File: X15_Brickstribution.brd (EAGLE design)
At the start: 152.4 x 76.2 mm, 77 parts, among them J1 IPL1-104-01-X-S-K, U5 IC_L4970A, U6 DIODE_STPS1545CT, U7 IC_L4970A, U8 DIODE_STPS1545CT

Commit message: In progress board
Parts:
- removed R31: DIODE_RBQ30NS45AFHTL, X15_Brickstribution:TRANS_R5009FNJ_ROM
- removed REV_TRANS: TRANS_IRF1018E_S_SLPBF, X15_Brickstribution:IRF1018E_S_SLPBF
- added R2: DIODE_RBQ30NS45AFHTL, X15_Brickstribution:TRANS_R5009FNJ_ROM
- added U$3: TRANS_IRF1018EPBF, X15_Brickstribution:D2PAK
- moved R21 115.0 mm to (177.6, 4.19), turned to 270 degrees
- moved C30 113.2 mm to (184.8, 16.0)
- moved D14 113.2 mm to (176.5, 7.11)
- moved R8 113.2 mm to (161.5, 63.8)
- moved +7.4VOUT1_TEST 113.2 mm to (206.0, 63.8)
- moved +7.4VOUT2_TEST 113.2 mm to (202.2, 63.7)
- moved 48V_GND_TEST 113.2 mm to (153.5, 63.7)
- moved 48V_TEST 113.2 mm to (166.9, 63.7)
- moved D12 113.2 mm to (172.9, 4.75)
- moved D13 113.2 mm to (200.7, 38.0)
- moved D8 113.2 mm to (157.8, 63.8)
- moved R22 113.2 mm to (201.5, 35.1)
- moved R12 112.7 mm to (175.9, 9.14)
- moved C38 69.4 mm to (27.9, 49.4), turned to 180 degrees
- moved C39 66.3 mm to (32.8, 41.0), turned to 0 degrees
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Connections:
- net +12V_CONV: no longer U5.9, U7.9
- net +48V: now also C1.1, C2.1, C3.1, U5.9, U7.9; no longer C1.2, C2.2, C3.2
- net +7.4V_SERVO: now also R2.2; no longer R31.2
- net 12V_GND: no longer 7.4V_GND.1, C23.1, C24.1, C26.1, C27.1, C28.1, C29.2, C30.1, C32.1, C33.1, C35.1, C36.1, C37.1, C38.2, C39.1, D12.C, D14.C, J1.03, J1.04, R23.1, R24.1, R26.1, R27.1, R28.1, R30.1, U5.3, U5.8, U6.1, U6.3, U7.3, U7.8, U8.1, U8.3
- net 48V_GND: now also 7.4V_GND.1, C1.2, C2.2, C23.1, C24.1, C26.1, C27.1, C28.1, C29.2, C3.2, C30.1, C32.1, C33.1, C35.1, C36.1, C37.1, C38.2, C39.1, D12.C, D14.C, J1.03, J1.04, R23.1, R24.1, R26.1, R27.1, R28.1, R30.1, U$3.2, U5.16, U5.3, U5.8, U6.1, U6.3, U7.16, U7.3, U7.8, U8.1, U8.3; no longer C1.1, C2.1, C3.1, REV_TRANS.P$3
- net GND_RAW: now also U$3.3; no longer REV_TRANS.P$2
- net REV_GATE: now also U$3.1; no longer REV_TRANS.P$1
- net VOUT1: now also R2.3; no longer R31.3
- net VOUT2: now also R2.1; no longer R31.1
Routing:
- net VOUT1: track 98.4 -> 15.0 mm, vias 1 -> 0
- net VOUT2: track 114.0 -> 45.0 mm, vias 1 -> 0
- net +3.3V: track 49.1 -> 0.00 mm
- net OUT2: track 84.0 -> 39.9 mm
- net +5V: track 35.8 -> 0.00 mm
- net OUT1: track 80.8 -> 55.1 mm
- net 48V_GND: track 3.57 -> 12.8 mm, vias 0 -> 3
- net +12V_CONV: track 8.76 -> 0.00 mm, vias 1 -> 0
- net BOOT2: track 20.8 -> 15.0 mm
- net FCOMP2: track 15.4 -> 20.0 mm
- net +12V: track 4.19 -> 0.00 mm
- net SS1: track 22.0 -> 25.6 mm
- net BOOT_1: track 10.8 -> 13.7 mm
- net C_OSC2: track 26.4 -> 23.7 mm
- net VSTART1: track 5.71 -> 3.21 mm
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- added copper zone on layer 1, net 48V_GND
- removed copper zone on layer 16, net +7.4V_SERVO
- removed copper zone on layer 1, net 12V_GND
- removed copper zone on layer 16, net 48V_GND

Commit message: Finished version of alternative layout
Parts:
- moved +7.4VOUT1_TEST 206.1 mm to (2.29, 32.8)
- moved +7.4VOUT2_TEST 157.8 mm to (44.7, 74.1)
- moved D14 151.3 mm to (25.3, 15.2)
- moved R12 146.3 mm to (29.8, 15.2), turned to 180 degrees
- moved C30 142.7 mm to (42.2, 21.7), turned to 180 degrees
- moved R21 141.5 mm to (36.8, 17.1), turned to 90 degrees
- moved D12 138.2 mm to (35.7, 21.3)
- moved D8 118.4 mm to (40.9, 44.7)
- moved R8 117.6 mm to (45.4, 44.7)
- moved R22 102.3 mm to (99.3, 31.6), turned to 270 degrees
- moved D13 102.0 mm to (99.3, 27.1), turned to 270 degrees
- moved 48V_TEST 89.3 mm to (78.3, 74.1)
- moved 48V_GND_TEST 70.9 mm to (83.4, 74.1)
- moved +7.4V_SERVO_TEST 14.5 mm to (28.8, 2.62)
- moved U$2 9.65 mm to (44.6, 67.6)
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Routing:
- net VOUT1: track 15.0 -> 63.2 mm, vias 0 -> 1
- net +3.3V: track 0.00 -> 45.1 mm
- net +5V: track 0.00 -> 42.8 mm
- net 48V_GND: track 12.8 -> 50.0 mm, vias 3 -> 6
- net VOUT2: track 45.0 -> 73.0 mm, vias 0 -> 2
- net OUT2: track 39.9 -> 54.4 mm, vias 0 -> 2
- net +12V_CONV: track 0.00 -> 5.06 mm, vias 0 -> 1
- net +12V: track 0.00 -> 4.92 mm
- net +48V: track 6.06 -> 10.6 mm
- net N$12: track 0.00 -> 3.32 mm
- net N$13: track 0.00 -> 2.82 mm
- net N$11: track 0.00 -> 2.74 mm
- net N$4: track 0.00 -> 2.74 mm
- net VREF1: track 9.62 -> 11.8 mm
- net N$9: track 0.00 -> 2.11 mm
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- added copper zone on layer 1, net +7.4V_SERVO
- added copper zone on layer 1, net 12V_GND

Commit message: Alumni Revisions Implemented
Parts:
- removed D2: SK34A-TPDO-214AC_HSMA_MCC-M, X15_Brickstribution:DO-214AC_HSMA_MCC-M
- removed D9: GREEN, SparkFun-LED:LED-0603
- removed R9: 470, SparkFun-Resistors:0603
- added CR1: Zener, X15_Brickstribution:DIODE_DO-214AA_4P38X3P62_MCC-M
- moved 12V_GND_TEST 37.0 mm to (150.3, 37.3)
- moved +12V_TEST 35.0 mm to (150.1, 33.7)
- moved 3.3V_GND 17.0 mm to (150.2, 30.4)
- moved 5V_GND 12.7 mm to (150.2, 23.2)
- moved +3.3V_TEST 3.30 mm to (150.1, 26.3)
- moved D10 0.76 mm to (142.4, 8.86)
- moved D11 0.76 mm to (139.8, 8.86)
- moved R10 0.51 mm to (142.4, 13.0)
- moved R11 0.51 mm to (139.8, 13.0)
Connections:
- removed net +12V_CONV: +12V_TEST.1, BACKPLANE_CONN.07, BACKPLANE_POWER.1@1, BACKPLANE_POWER.1@2, BACKPLANE_POWER.1@3, BACKPLANE_POWER.1@4, BACKPLANE_POWER.1@5, BACKPLANE_POWER.1@6, BACKPLANE_POWER.2@1, BACKPLANE_POWER.2@2, BACKPLANE_POWER.2@3, BACKPLANE_POWER.2@4, BACKPLANE_POWER.2@5, BACKPLANE_POWER.2@6, BACKPLANE_POWER.3@1, BACKPLANE_POWER.3@2, BACKPLANE_POWER.3@3, BACKPLANE_POWER.3@4, BACKPLANE_POWER.3@5, BACKPLANE_POWER.3@6, BACKPLANE_POWER.4@1, BACKPLANE_POWER.4@2, BACKPLANE_POWER.4@3, BACKPLANE_POWER.4@4, BACKPLANE_POWER.4@5, BACKPLANE_POWER.4@6, BACKPLANE_POWER.5@1, BACKPLANE_POWER.5@2, BACKPLANE_POWER.5@3, BACKPLANE_POWER.5@4, BACKPLANE_POWER.5@5, BACKPLANE_POWER.5@6, D2.1, R9.1, U$1.1, U$1.2
- removed net N$8: D9.A, R9.2
- net +12V: now also +12V_TEST.1, BACKPLANE_CONN.07, BACKPLANE_POWER.1@1, BACKPLANE_POWER.1@2, BACKPLANE_POWER.1@3, BACKPLANE_POWER.1@4, BACKPLANE_POWER.1@5, BACKPLANE_POWER.1@6, BACKPLANE_POWER.2@1, BACKPLANE_POWER.2@2, BACKPLANE_POWER.2@3, BACKPLANE_POWER.2@4, BACKPLANE_POWER.2@5, BACKPLANE_POWER.2@6, BACKPLANE_POWER.3@1, BACKPLANE_POWER.3@2, BACKPLANE_POWER.3@3, BACKPLANE_POWER.3@4, BACKPLANE_POWER.3@5, BACKPLANE_POWER.3@6, BACKPLANE_POWER.4@1, BACKPLANE_POWER.4@2, BACKPLANE_POWER.4@3, BACKPLANE_POWER.4@4, BACKPLANE_POWER.4@5, BACKPLANE_POWER.4@6, BACKPLANE_POWER.5@1, BACKPLANE_POWER.5@2, BACKPLANE_POWER.5@3, BACKPLANE_POWER.5@4, BACKPLANE_POWER.5@5, BACKPLANE_POWER.5@6, CR1.1, U$1.1, U$1.2, U$1.3, U$1.4; no longer D2.2
- net 12V_GND: now also CR1.2; no longer D9.C, U$1.3, U$1.4
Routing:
- net +3.3V: track 45.1 -> 50.6 mm
- net +12V_CONV: track 5.06 -> 0.00 mm, vias 1 -> 0
- net +12V: track 4.92 -> 8.91 mm
- net N$8: track 1.88 -> 0.00 mm
- net +5V: track 42.8 -> 43.3 mm
- removed copper zone on layer 16, net +12V_CONV

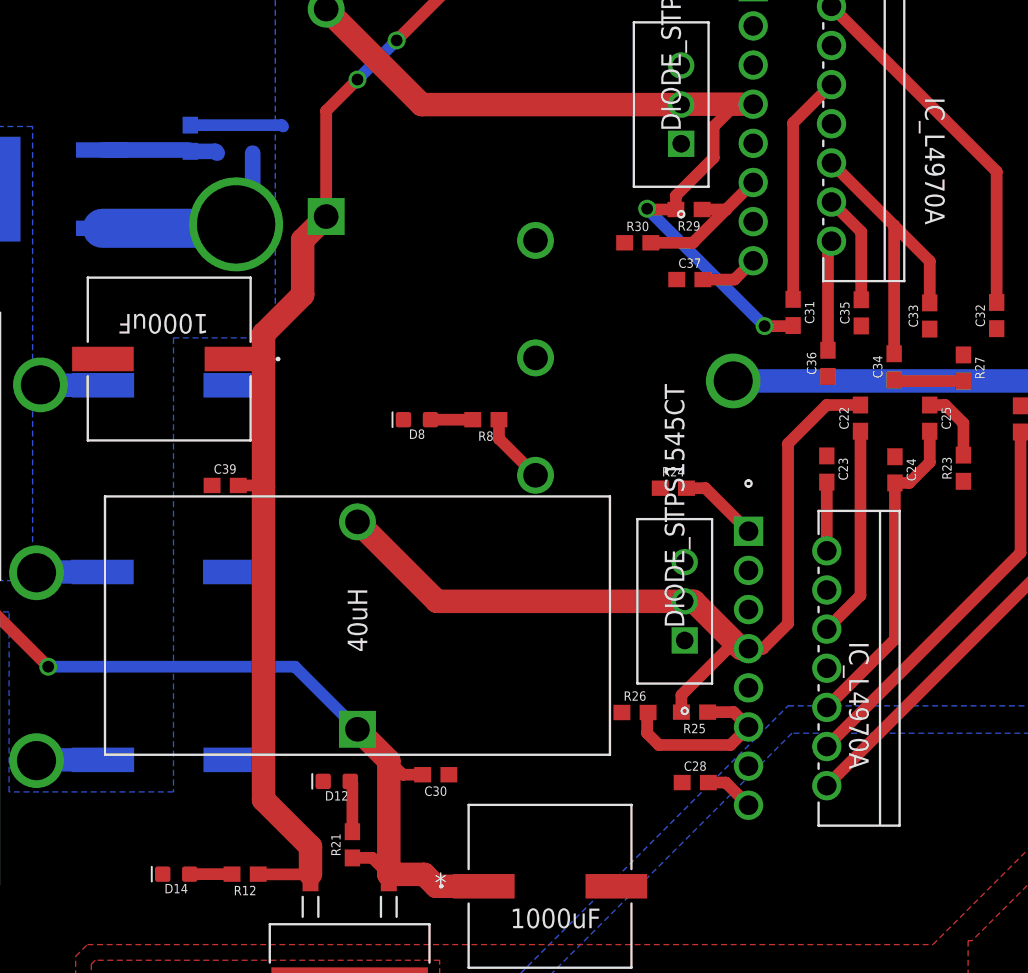
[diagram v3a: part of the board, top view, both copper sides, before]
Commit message: Fixed Tracing Errors
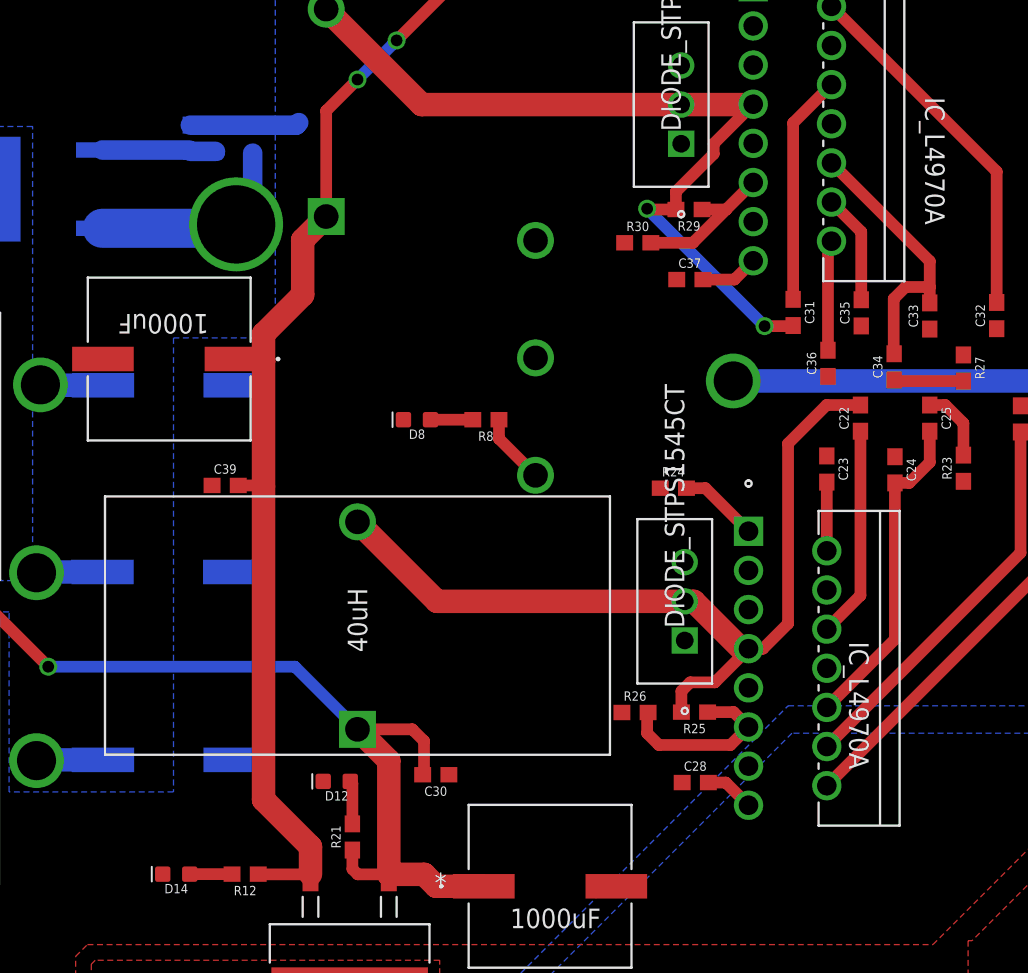
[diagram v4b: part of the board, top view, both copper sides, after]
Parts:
- moved R21 0.51 mm to (36.8, 17.7)
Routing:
- net VOUT1: track 63.2 -> 65.5 mm
- net FCOMP2: track 20.0 -> 18.0 mm
- net +48V: track 10.6 -> 11.7 mm
- net OUT2: track 54.4 -> 53.7 mm
- net OUT1: track 55.7 -> 56.3 mm
- net N$12: track 3.32 -> 2.81 mm
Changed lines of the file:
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@@
 <attribute name="VALUE" x="27.4828" y="1.0922" size="0.6096" layer="27" font="vector" ratio="20" align="top-left"/>
 </element>
-<element name="R21" library="SparkFun-Resistors" library_urn="urn:adsk.eagle:library:532" package="0603" package3d_urn="urn:adsk.eagle:package:39650/1" value="470" x="36.7538" y="17.145" smashed="yes" rot="R90">
-<attribute name="NAME" x="35.9918" y="17.145" size="0.6096" layer="25" font="vector" ratio="20" rot="R90" align="bottom-center"/>
-<attribute name="PROD_ID" value="RES-07869" x="36.7538" y="18.415" size="1.778" layer="27" rot="R90" display="off"/>
-<attribute name="VALUE" x="37.5158" y="17.145" size="0.6096" layer="27" font="vector" ratio="20" rot="R90" align="top-center"/>
+<element name="R21" library="SparkFun-Resistors" library_urn="urn:adsk.eagle:library:532" package="0603" package3d_urn="urn:adsk.eagle:package:39650/1" value="470" x="36.7538" y="17.653" smashed="yes" rot="R90">
+<attribute name="NAME" x="35.9918" y="17.653" size="0.6096" layer="25" font="vector" ratio="20" rot="R90" align="bottom-center"/>
+<attribute name="PROD_ID" value="RES-07869" x="36.7538" y="18.923" size="1.778" layer="27" rot="R90" display="off"/>
+<attribute name="VALUE" x="37.5158" y="17.653" size="0.6096" layer="27" font="vector" ratio="20" rot="R90" align="top-center"/>
 </element>
 <element name="D12" library="SparkFun-LED" library_urn="urn:adsk.eagle:library:529" package="LED-0603" package3d_urn="urn:adsk.eagle:package:39354/1" value="GREEN" x="35.7378" y="21.2598" smashed="yes" rot="R180">
@@
 <vertex x="14.478" y="32.258"/>
 </polygon>
-<wire x1="26.2382" y1="63.842" x2="32.17" y2="63.842" width="0.762" layer="16"/>
-<wire x1="32.17" y1="63.842" x2="32.258" y2="63.754" width="0.762" layer="16"/>
 <wire x1="48.637" y1="41.1202" x2="46.2652" y2="43.492" width="0.762" layer="1"/>
 <wire x1="46.2652" y1="43.492" x2="46.2652" y2="44.7294" width="0.762" layer="1"/>
+<wire x1="26.2382" y1="63.842" x2="33.108" y2="63.842" width="1.27" layer="16"/>
+<wire x1="33.108" y1="63.842" x2="33.274" y2="64.008" width="1.27" layer="16"/>
 </signal>
 <signal name="48V_GND">
@@
 <wire x1="20.522" y1="57.15" x2="28.956" y2="57.15" width="2.54" layer="16"/>
 <wire x1="28.956" y1="57.15" x2="29.21" y2="57.404" width="2.54" layer="16"/>
-<wire x1="30.2838" y1="62.0268" x2="30.2838" y2="58.4778" width="1.016" layer="16"/>
-<wire x1="30.2838" y1="58.4778" x2="28.956" y2="57.15" width="1.016" layer="16"/>
 <wire x1="20.566896875" y1="46.9646" x2="16.5354" y2="46.9646" width="1.524" layer="16"/>
 <wire x1="20.541496875" y1="34.8488" x2="16.3068" y2="34.8488" width="1.524" layer="16"/>
@@
 <vertex x="96.012" y="32.258"/>
 </polygon>
+<wire x1="29.21" y1="57.404" x2="30.2838" y2="58.4778" width="1.27" layer="16"/>
+<wire x1="30.2838" y1="58.4778" x2="30.2838" y2="62.0268" width="1.27" layer="16"/>
 </signal>
 <signal name="12V_GND">
@@
 <contactref element="U$3" pad="1"/>
 <wire x1="26.1502" y1="62.23" x2="26.2382" y2="62.142" width="0.762" layer="16"/>
-<wire x1="20.522" y1="62.23" x2="26.1502" y2="62.23" width="1.016" layer="16"/>
-<wire x1="26.2382" y1="62.142" x2="27.8686" y2="62.142" width="1.016" layer="16"/>
 <wire x1="27.8686" y1="62.142" x2="27.9838" y2="62.0268" width="1.016" layer="16"/>
+<wire x1="20.522" y1="62.23" x2="26.1502" y2="62.23" width="1.27" layer="16"/>
+<wire x1="26.2382" y1="62.142" x2="27.8686" y2="62.142" width="1.27" layer="16"/>
 </signal>
 <signal name="GND_RAW">
@@
 <contactref element="C33" pad="2"/>
 <contactref element="C34" pad="2"/>
-<wire x1="67.8434" y1="61.3918" x2="71.9074" y2="57.3278" width="0.762" layer="1"/>
-<wire x1="71.9074" y1="57.3278" x2="71.9074" y2="49.0084" width="0.762" layer="1"/>
-<wire x1="71.9074" y1="57.3278" x2="74.2188" y2="55.0164" width="0.762" layer="1"/>
-<wire x1="74.2188" y1="55.0164" x2="74.2188" y2="52.3104" width="0.762" layer="1"/>
+<wire x1="67.8434" y1="61.3918" x2="74.2188" y2="55.0164" width="0.762" layer="1"/>
+<wire x1="74.2188" y1="55.0164" x2="74.2188" y2="53.34" width="0.762" layer="1"/>
+<wire x1="74.2188" y1="53.34" x2="74.2188" y2="52.3104" width="0.762" layer="1"/>
+<wire x1="74.2188" y1="53.34" x2="72.644" y2="53.34" width="0.762" layer="1"/>
+<wire x1="72.644" y1="53.34" x2="71.882" y2="52.578" width="0.762" layer="1"/>
+<wire x1="71.882" y1="52.578" x2="71.882" y2="49.0338" width="0.762" layer="1"/>
+<wire x1="71.882" y1="49.0338" x2="71.9074" y2="49.0084" width="0.762" layer="1"/>
 </signal>
 <signal name="R_OSC2">
@@
 <contactref element="L2" pad="2"/>
 <contactref element="R29" pad="2"/>
-<wire x1="57.7478" y1="58.3692" x2="57.7478" y2="59.2718" width="0.762" layer="1"/>
-<wire x1="57.7478" y1="59.2718" x2="60.198" y2="61.722" width="0.762" layer="1"/>
-<wire x1="60.198" y1="61.722" x2="60.198" y2="63.754" width="0.762" layer="1"/>
-<wire x1="60.198" y1="63.754" x2="61.6458" y2="65.2018" width="0.762" layer="1"/>
-<wire x1="61.6458" y1="65.2018" x2="62.7634" y2="65.2018" width="0.762" layer="1"/>
-<wire x1="62.7634" y1="65.2018" x2="58.1152" y2="65.2018" width="1.524" layer="1"/>
-<wire x1="58.1152" y1="65.2018" x2="58.0898" y2="65.1764" width="1.524" layer="1"/>
 <wire x1="58.0898" y1="65.1764" x2="41.2496" y2="65.1764" width="1.524" layer="1"/>
 <wire x1="41.2496" y1="65.1764" x2="35.052" y2="71.374" width="1.524" layer="1"/>
@@
 <wire x1="63.5" y1="50.8" x2="65.3152" y2="50.8" width="0.762" layer="1"/>
 <wire x1="65.3152" y1="50.8" x2="65.3542" y2="50.839" width="0.762" layer="1"/>
+<wire x1="62.738" y1="65.1764" x2="60.198" y2="62.6364" width="0.762" layer="1"/>
+<wire x1="60.198" y1="62.6364" x2="60.198" y2="61.976" width="0.762" layer="1"/>
+<wire x1="60.198" y1="61.976" x2="57.7478" y2="59.5258" width="0.762" layer="1"/>
+<wire x1="57.7478" y1="59.5258" x2="57.7478" y2="58.3692" width="0.762" layer="1"/>
+<wire x1="62.738" y1="65.1764" x2="62.7634" y2="65.2018" width="1.524" layer="1"/>
+<wire x1="58.0898" y1="65.1764" x2="62.738" y2="65.1764" width="1.524" layer="1"/>
 </signal>
 <signal name="VSTART2">
@@
 <wire x1="37.084" y1="24.638" x2="39.116" y2="22.606" width="1.524" layer="1"/>
 <wire x1="39.116" y1="22.606" x2="39.116" y2="15.2273" width="1.524" layer="1"/>
-<wire x1="37.084" y1="24.638" x2="40.0304" y2="21.6916" width="0.762" layer="1"/>
-<wire x1="40.0304" y1="21.6916" x2="41.314" y2="21.6916" width="0.762" layer="1"/>
 <wire x1="37.084" y1="24.638" x2="33.02" y2="28.702" width="0.762" layer="16"/>
 <wire x1="33.02" y1="28.702" x2="17.018" y2="28.702" width="0.762" layer="16"/>
@@
 <wire x1="17.018" y1="28.702" x2="12.9286" y2="32.7914" width="0.762" layer="1"/>
 <wire x1="12.9286" y1="32.7914" x2="2.286" y2="32.7914" width="0.762" layer="1"/>
-<wire x1="39.116" y1="15.2273" x2="38.0483" y2="16.295" width="0.762" layer="1"/>
-<wire x1="38.0483" y1="16.295" x2="36.7538" y2="16.295" width="0.762" layer="1"/>
 <wire x1="39.116" y1="15.2273" x2="41.4147" y2="15.2273" width="1.524" layer="1"/>
 <wire x1="42.1894" y1="14.4526" x2="45.281096875" y2="14.4526" width="1.524" layer="1"/>
 <wire x1="41.4147" y1="15.2273" x2="42.1894" y2="14.4526" width="1.524" layer="1"/>
+<wire x1="37.084" y1="24.638" x2="40.64" y2="24.638" width="0.762" layer="1"/>
+<wire x1="40.64" y1="24.638" x2="41.402" y2="23.876" width="0.762" layer="1"/>
+<wire x1="41.402" y1="23.876" x2="41.402" y2="21.7796" width="0.762" layer="1"/>
+<wire x1="41.402" y1="21.7796" x2="41.314" y2="21.6916" width="0.762" layer="1"/>
+<wire x1="39.116" y1="15.2273" x2="37.0967" y2="15.2273" width="0.762" layer="1"/>
+<wire x1="36.7538" y1="15.5702" x2="36.7538" y2="16.803" width="0.762" layer="1"/>
+<wire x1="37.0967" y1="15.2273" x2="36.7538" y2="15.5702" width="0.762" layer="1"/>
 </signal>
 <signal name="VREF1">
@@
 <wire x1="42.2402" y1="32.9438" x2="37.084" y2="38.1" width="1.524" layer="1"/>
 <wire x1="62.4586" y1="29.8704" x2="61.976" y2="29.8704" width="0.762" layer="1"/>
-<wire x1="61.976" y1="29.8704" x2="61.1124" y2="29.8704" width="0.762" layer="1"/>
-<wire x1="58.1034" y1="26.8614" x2="58.1034" y2="25.7556" width="0.762" layer="1"/>
-<wire x1="61.1124" y1="29.8704" x2="58.1034" y2="26.8614" width="0.762" layer="1"/>
 <wire x1="58.3184" y1="32.9438" x2="58.9026" y2="32.9438" width="1.524" layer="1"/>
 <wire x1="58.9026" y1="32.9438" x2="61.976" y2="29.8704" width="1.524" layer="1"/>
+<wire x1="62.4586" y1="29.8704" x2="60.2742" y2="27.686" width="0.762" layer="1"/>
+<wire x1="60.2742" y1="27.686" x2="58.674" y2="27.686" width="0.762" layer="1"/>
+<wire x1="58.674" y1="27.686" x2="58.1034" y2="27.1154" width="0.762" layer="1"/>
+<wire x1="58.1034" y1="27.1154" x2="58.1034" y2="25.7556" width="0.762" layer="1"/>
 </signal>
 <signal name="VSTART1">
@@
 <contactref element="R21" pad="2"/>
 <contactref element="D12" pad="A"/>
-<wire x1="36.7538" y1="17.995" x2="36.7538" y2="21.1208" width="0.762" layer="1"/>
+<wire x1="36.7538" y1="18.503" x2="36.7538" y2="21.1208" width="0.762" layer="1"/>
 <wire x1="36.7538" y1="21.1208" x2="36.6148" y2="21.2598" width="0.762" layer="1"/>
 </signal>

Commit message: Final Iteration of Layout
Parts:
- removed D12: GREEN, SparkFun-LED:LED-0603
- removed D14: RED, SparkFun-LED:LED-0603
- removed R10: 150, SparkFun-Resistors:0603
- removed R11: 100, SparkFun-Resistors:0603
- removed R12, R21, R22: 470, SparkFun-Resistors:0603
- added D2, D3: Yellow, SparkFun-LED:LED-0603
- added R3: 1.5k, SparkFun-Resistors:0603
- added R4: 100, SparkFun-Resistors:0603
- added R5, R6: 150, SparkFun-Resistors:0603
- added R7: 470, SparkFun-Resistors:0603
- R8: value 2.49k -> 20
- moved R8 99.3 mm to (139.4, 12.7), turned to 270 degrees
- moved D13 0.51 mm to (99.3, 26.5)
- moved D11 0.25 mm to (139.5, 8.86)
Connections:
- net +12V: now also R7.1; no longer R22.1
- net +3.3V: now also R8.1; no longer R11.1
- net +48V: now also R3.1; no longer R8.1
- net +5V: now also R4.1; no longer R10.1
- net 48V_GND: now also D2.C, D3.C; no longer D12.C, D14.C
- net N$10: now also R8.2; no longer R11.2
- net N$11: now also D3.A, R6.2; no longer D14.A, R12.2
- net N$12: now also D2.A, R5.2; no longer D12.A, R21.2
- net N$13: now also R7.2; no longer R22.2
- net N$4: now also R3.2; no longer R8.2
- net N$9: now also R4.2; no longer R10.2
- net VOUT1: now also R5.1; no longer R21.1
- net VOUT2: now also R6.1; no longer R12.1
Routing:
- net 48V_GND: track 49.6 -> 63.1 mm, vias 6 -> 7
- net +12V: track 8.91 -> 10.3 mm
- net FCOMP2: track 18.0 -> 16.9 mm
- net N$13: track 2.82 -> 1.97 mm
- net N$12: track 2.81 -> 2.26 mm
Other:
- board text added: "+"
- board text added: "-"
- board text added: "12V LED"
- board text added: "3.3V LED"
- board text added: "48V LED"
- board text added: "5V LED"
- board text added: "7.4V LED #1"
- board text added: "7.4V LED #2"
- board text added: "X15 Brickstribution Ayman Motoda Minh Nguyen Bryce Sasser Rachel Livesay Katherine Sandys"

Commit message: Revision before implementing Samtec Brick Connectors
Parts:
- C1, C2, C3: value 0.330mF -> 330uF; device X15_Brickstribution:CAP_MZR_JA0_NIP-M -> X15_Brickstribution:CAP_099112E3_VIS-M
- CR1: value Zener -> DIODE(Z)_SMBJ5357B-TPDIODE_DO-214AA_4P38X3P62_MCC-M
- U$3: value TRANS_IRF1018EPBF -> TRANS_IRF1018ESTRLPBF
- moved C1 25.6 mm to (25.1, 48.3)
- moved C3 14.8 mm to (25.1, 20.1)
- moved C2 12.4 mm to (25.1, 34.5)
- moved L2 3.31 mm to (37.8, 59.7)
- moved TETHER_48V 2.17 mm to (7.47, 17.9)
- moved TETHER_GND 2.17 mm to (7.54, 48.3)
- moved U$3 1.70 mm to (12.4, 60.5)
- moved D1 0.80 mm to (28.9, 62.8)
- moved R1 0.80 mm to (26.0, 63.8)
- moved C24 0.76 mm to (72.0, 40.7)
- moved C23 0.51 mm to (67.5, 41.0)
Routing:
- net 48V_GND: track 63.1 -> 87.1 mm, vias 7 -> 9
- net 12V_GND: track 0.00 -> 6.47 mm
- net OUT2: track 53.7 -> 51.6 mm
- net +48V: track 11.7 -> 13.5 mm
- net REV_GATE: track 7.55 -> 8.82 mm
- net C_OSC1: track 4.46 -> 3.95 mm
